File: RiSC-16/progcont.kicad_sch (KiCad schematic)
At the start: 9 parts, among them U6 74LS373, U7 74LS257, U8 74LS373, U9 74LS257

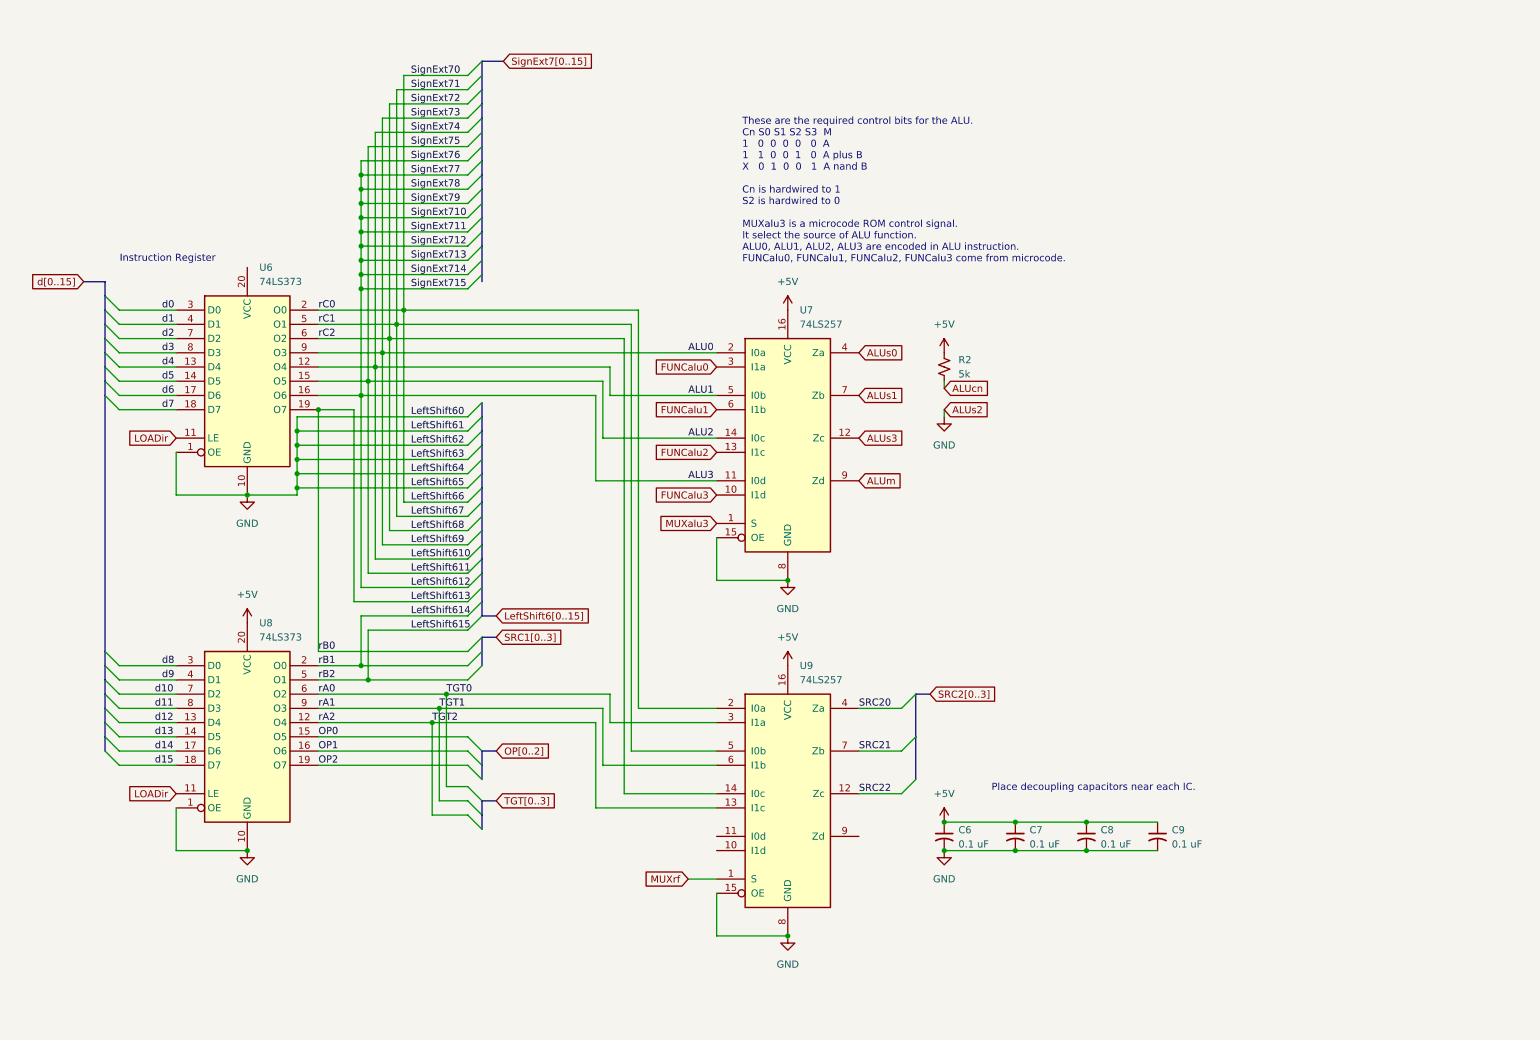
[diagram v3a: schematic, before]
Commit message: Refined instruction register.
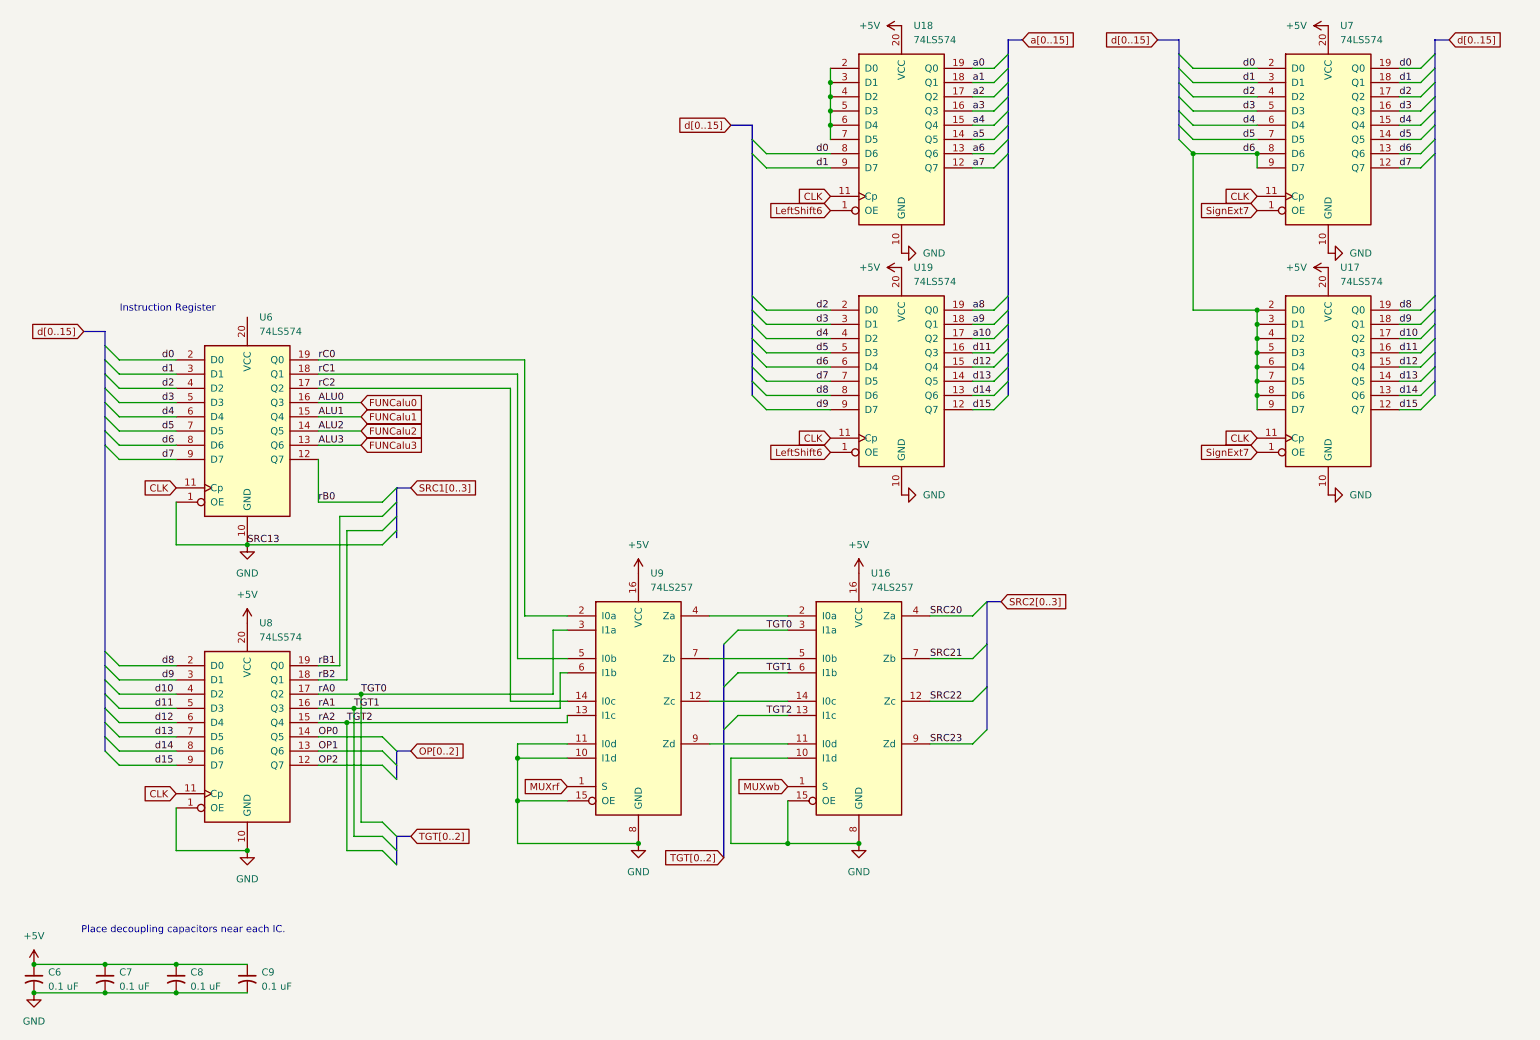
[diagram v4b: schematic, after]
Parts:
- removed R2: 5k, symbol Device:R_Small_US
- removed U6, U8: 74LS373, symbol 74xx:74LS373
- removed U7: 74LS257, symbol 74xx:74LS257
- added U16: 74LS257, symbol 74xx:74LS257
- added U17, U18, U19, U6, U7, U8: 74LS574, symbol 74xx:74LS574
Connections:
- net +5V: now also U16.16 (VCC), U17.20 (VCC), U18.20 (VCC), U19.20 (VCC), U7.20 (VCC), U8.20 (VCC)
- net FUNCalu0: now also U6.16 (Q3)
- net FUNCalu1: now also U6.15 (Q4)
- net FUNCalu2: now also U6.14 (Q5)
- net FUNCalu3: now also U6.13 (Q6)
- net GND: now also U9.10 (I1d), U9.11 (I0d), U16.10 (I1d), U16.15 (OE), U16.8 (GND), U17.10 (GND), U18.10 (GND), U19.10 (GND), U6.1 (OE), U6.10 (GND), U7.10 (GND), U8.1 (OE), U8.10 (GND)
- net OP0: now also U8.14 (Q5)
- net OP1: now also U8.13 (Q6)
- net OP2: now also U8.12 (Q7)
- net SRC20: now also U16.4 (Za); no longer U9.4 (Za)
- net SRC21: now also U16.7 (Zb); no longer U9.7 (Zb)
- net SRC22: now also U16.12 (Zc); no longer U9.12 (Zc)
- net TGT0: now also U16.3 (I1a), U8.17 (Q2)
- net TGT1: now also U16.6 (I1b), U8.16 (Q3)
- net TGT2: now also U16.13 (I1c), U8.15 (Q4)
- net d0: now also U18.8 (D6), U6.2 (D0), U7.19 (Q0), U7.2 (D0)
- net d1: now also U18.9 (D7), U6.3 (D1), U7.18 (Q1), U7.3 (D1)
- net d10: now also U17.17 (Q2), U8.4 (D2)
- net d11: now also U17.16 (Q3), U19.16 (Q3), U8.5 (D3)
- net d12: now also U17.15 (Q4), U19.15 (Q4), U8.6 (D4)
- net d13: now also U17.14 (Q5), U19.14 (Q5), U8.7 (D5)
- net d14: now also U17.13 (Q6), U19.13 (Q6), U8.8 (D6)
- net d15: now also U17.12 (Q7), U19.12 (Q7), U8.9 (D7)
- net d2: now also U19.2 (D0), U6.4 (D2), U7.17 (Q2), U7.4 (D2)
- net d3: now also U19.3 (D1), U6.5 (D3), U7.16 (Q3), U7.5 (D3)
- net d4: now also U19.4 (D2), U6.6 (D4), U7.15 (Q4), U7.6 (D4)
- net d5: now also U19.5 (D3), U6.7 (D5), U7.14 (Q5), U7.7 (D5)
- net d6: now also U17.2 (D0), U17.3 (D1), U17.4 (D2), U17.5 (D3), U17.6 (D4), U17.7 (D5), U17.8 (D6), U17.9 (D7), U19.6 (D4), U6.8 (D6), U7.13 (Q6), U7.8 (D6), U7.9 (D7)
- net d7: now also U19.7 (D5), U6.9 (D7), U7.12 (Q7)
- net d8: now also U17.19 (Q0), U19.8 (D6), U8.2 (D0)
- net d9: now also U17.18 (Q1), U19.9 (D7), U8.3 (D1)
- net at U9.9 (Zd): now also U16.11 (I0d)
- net LeftShift66 renamed rC0
- net rC0: now also U6.19 (Q0)
- net LeftShift67 renamed rC1
- net rC1: now also U6.18 (Q1)
- net LeftShift68 renamed rC2
- net rC2: now also U6.17 (Q2)
- new net: U18.2 (D0), U18.3 (D1), U18.4 (D2), U18.5 (D3), U18.6 (D4), U18.7 (D5)
- new net: U16.14 (I0c), U9.12 (Zc)
- new net: U16.2 (I0a), U9.4 (Za)
- new net: U16.5 (I0b), U9.7 (Zb)
- new net CLK: U17.11 (Cp), U18.11 (Cp), U19.11 (Cp), U6.11 (Cp), U7.11 (Cp), U8.11 (Cp)
- new net LeftShift6: U18.1 (OE), U19.1 (OE)
- new net MUXwb: U16.1 (S)
- new net SRC23: U16.9 (Zd)
- new net SignExt7: U17.1 (OE), U7.1 (OE)
- new net a0: U18.19 (Q0)
- new net a1: U18.18 (Q1)
- new net a10: U19.17 (Q2)
- new net a2: U18.17 (Q2)
- new net a3: U18.16 (Q3)
- new net a4: U18.15 (Q4)
- new net a5: U18.14 (Q5)
- new net a6: U18.13 (Q6)
- new net a7: U18.12 (Q7)
- new net a8: U19.19 (Q0)
- new net a9: U19.18 (Q1)
- new net rB0: U6.12 (Q7)
- new net rB1: U8.19 (Q0)
- new net rB2: U8.18 (Q1)
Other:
- note removed: "These are the required control bits for the ALU. Cn S0 S1 S2 S3 M 1 0 0 0 0 0 A 1 1 0 0 1 0 A plus B X 0 1 0 0 1 A nand B Cn is hardwired to 1 S2 is hardwired to 0 MUXalu3 is a microcode ROM control signal. It select the source of ALU function. ALU0, ALU1, ALU2, ALU3 are encoded in ALU instruction. FUNCalu0, FUNCalu1, FUNCalu2, FUNCalu3 come from microcode."
- moved on the sheet: C6, C7, C8, C9, U9

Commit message: Continued on the instruction register and decoding.
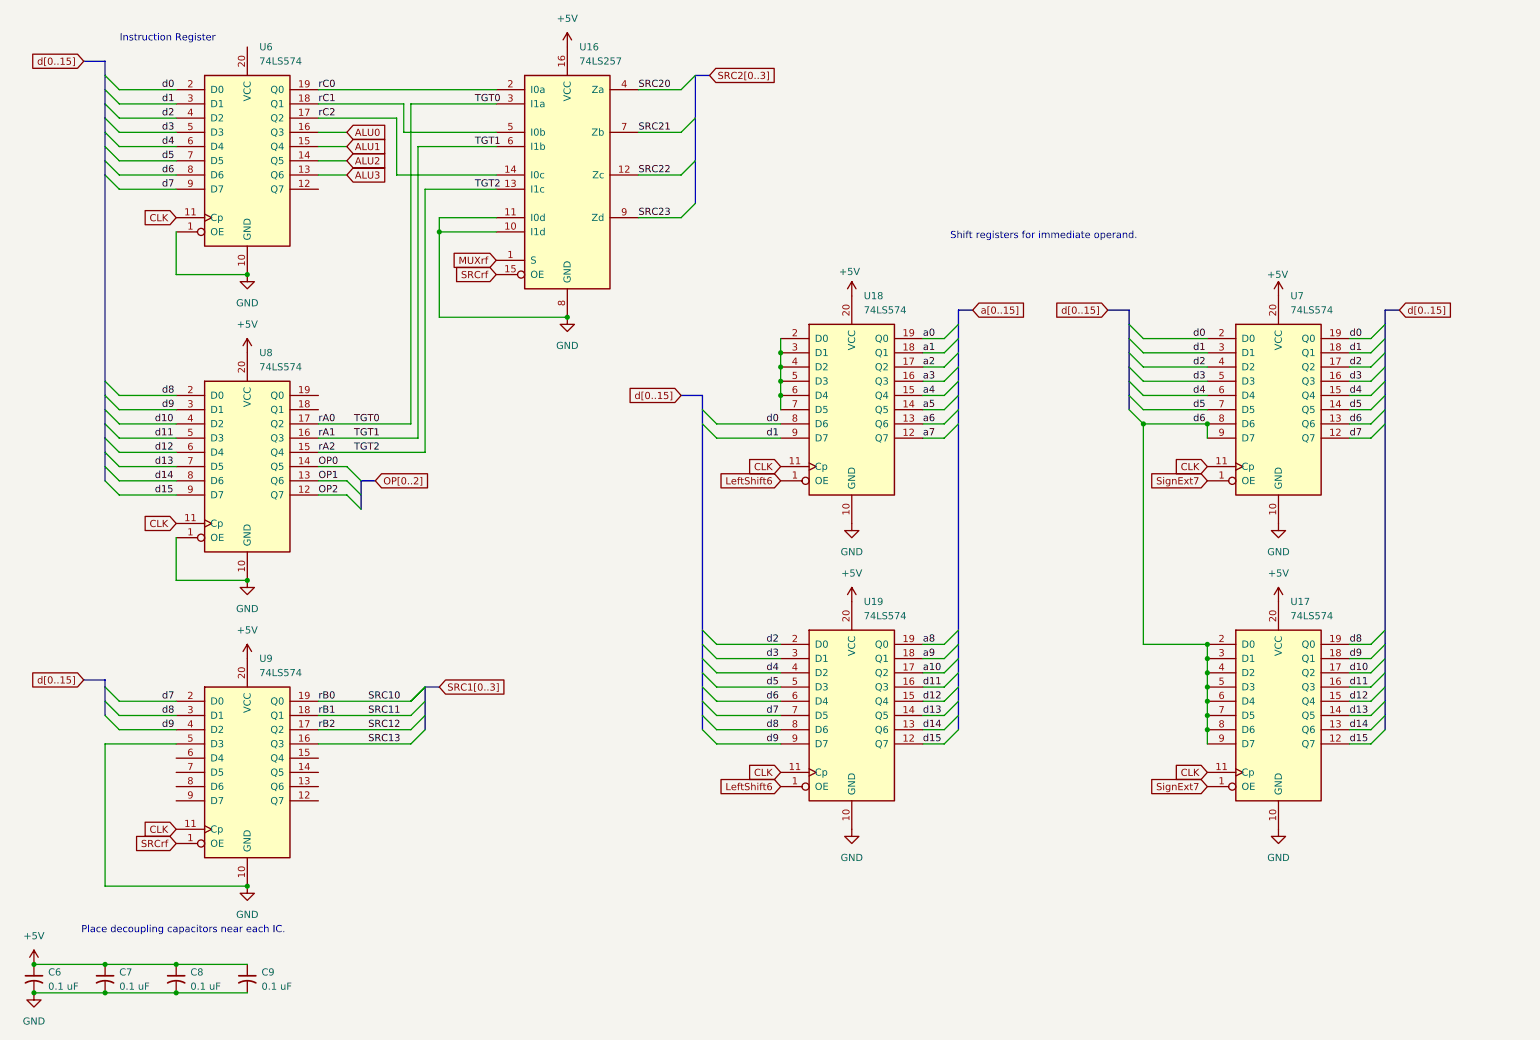
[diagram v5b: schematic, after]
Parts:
- removed U9: 74LS257, symbol 74xx:74LS257
- added U9: 74LS574, symbol 74xx:74LS574
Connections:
- net MUXwb is gone; now on net MUXrf: U16.1 (S)
- net +5V: now also U9.20 (VCC)
- net CLK: now also U9.11 (Cp)
- net GND: now also U16.11 (I0d), U9.10 (GND), U9.5 (D3); no longer U16.15 (OE)
- net d7: now also U9.2 (D0)
- net d8: now also U9.3 (D1)
- net d9: now also U9.4 (D2)
- net rC0: now also U16.2 (I0a)
- net rC1: now also U16.5 (I0b)
- net rC2: now also U16.14 (I0c)
- net FUNCalu0 renamed ALU0
- net FUNCalu1 renamed ALU1
- net FUNCalu2 renamed ALU2
- net FUNCalu3 renamed ALU3
- net rB0: no longer names the net of U6.12 (Q7)
- net rB1: no longer names the net of U8.19 (Q0)
- net rB2: no longer names the net of U8.18 (Q1)
- new net SRC10: U9.19 (Q0)
- new net SRC11: U9.18 (Q1)
- new net SRC12: U9.17 (Q2)
- new net SRC13: U9.16 (Q3)
- new net SRCrf: U16.15 (OE), U9.1 (OE)
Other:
- note added: "Shift registers for immediate operand."
- moved on the sheet: U16, U17, U18, U19, U6, U7, U8

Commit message: Annotated the schematic to align part numbers. EPROM and RAM board was added last revision. Reworked the src1 latching to assert 0xf to select the PC.
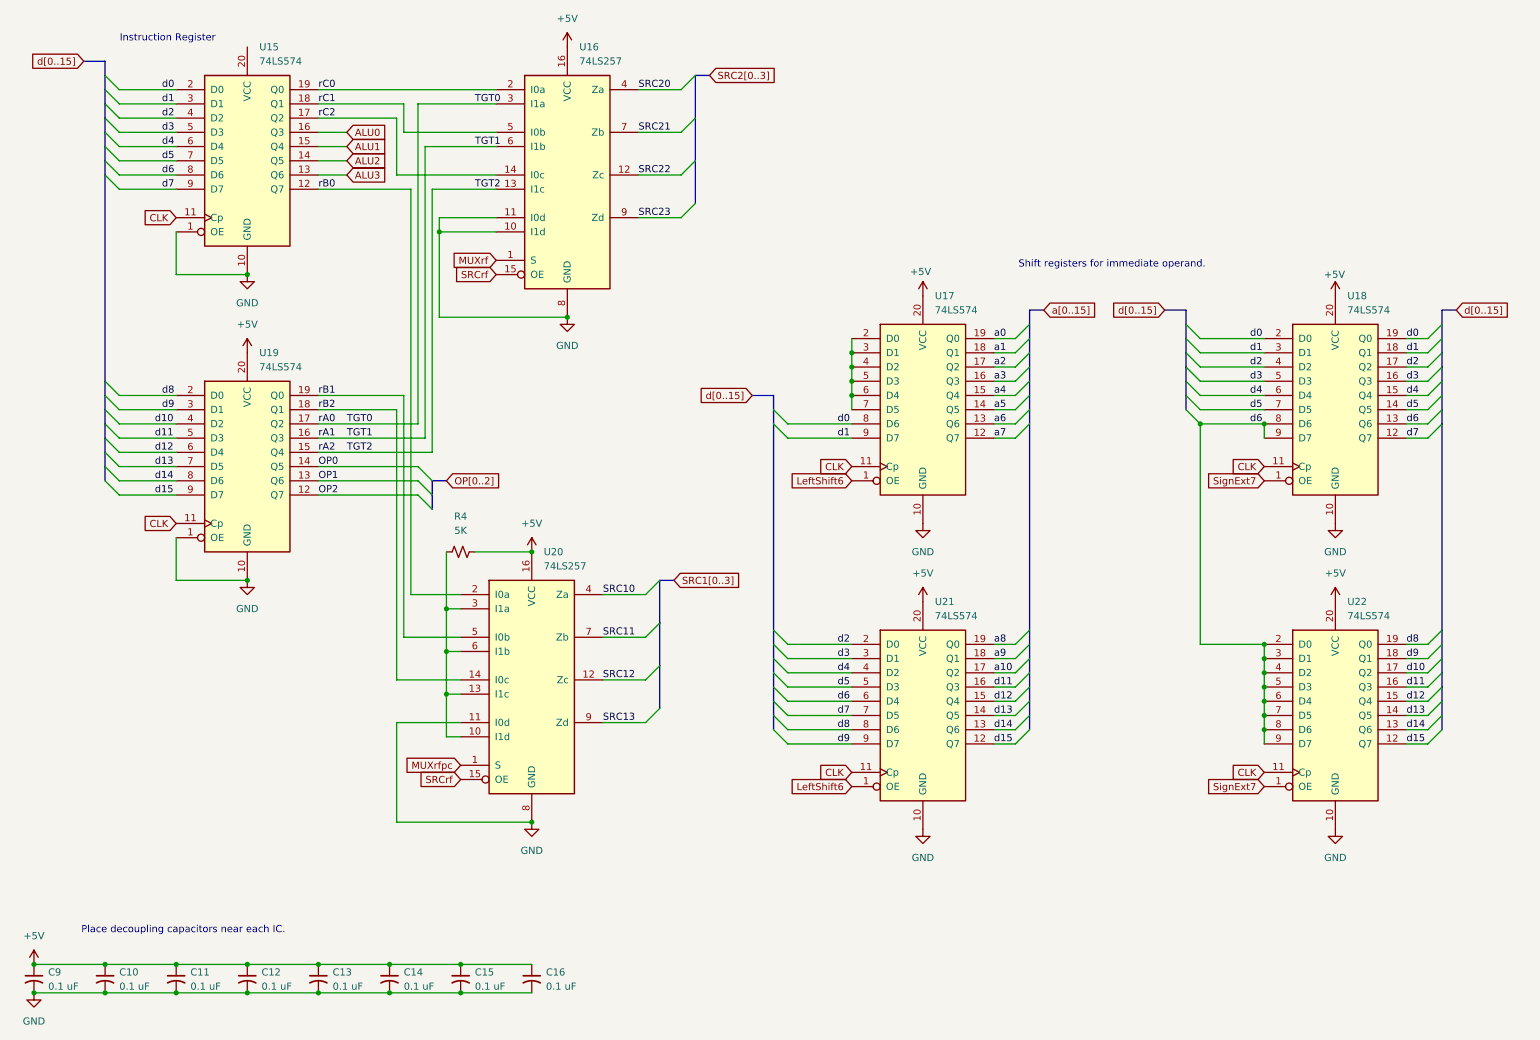
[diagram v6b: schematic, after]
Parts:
- removed U9: 74LS574, symbol 74xx:74LS574
- added C13, C14, C15, C16: 0.1 uF, symbol Device:C_Small_US
- added R4: 5K, symbol Device:R_Small_US
- added U20: 74LS257, symbol 74xx:74LS257
- renumbered C7 to C10, C8 to C11, C9 to C12, C6 to C9, U6 to U15, U18 to U17, U7 to U18, U8 to U19, U19 to U21, U17 to U22
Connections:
- net +5V: now also C13.1, C14.1, C15.1, C16.1, R4.1, U20.16 (VCC)
- net GND: now also C13.2, C14.2, C15.2, C16.2, U20.11 (I0d), U20.8 (GND)
- net SRC10: now also U20.4 (Za)
- net SRC11: now also U20.7 (Zb)
- net SRC12: now also U20.12 (Zc)
- net SRC13: now also U20.9 (Zd)
- net SRCrf: now also U20.15 (OE)
- net rB0: now reaches U15.12 (Q7)
- net rB0: now also U20.2 (I0a)
- net rB2: now reaches U19.18 (Q1)
- net rB2: now also U20.14 (I0c)
- net rB1: now reaches U19.19 (Q0)
- net rB1: now also U20.5 (I0b)
- new net: R4.2, U20.10 (I1d), U20.13 (I1c), U20.3 (I1a), U20.6 (I1b)
- new net MUXrfpc: U20.1 (S)
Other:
- moved on the sheet: U17, U18, U21, U22

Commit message: Minor edits
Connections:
- net at R4.2, U20.10 (I1d), U20.13 (I1c)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: no longer U20.3 (I1a)
- new net PCMAR: U20.3 (I1a)
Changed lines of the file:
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@@
 	)
 	(junction
-		(at 93.98 134.62)
-		(diameter 0)
-		(color 0 0 0 0)
-	)
-	(junction
 		(at 58.42 59.69)
 		(diameter 0)
@@
 	)
 	(junction
-		(at 93.98 127)
-		(diameter 0)
-		(color 0 0 0 0)
-	)
-	(junction
 		(at 71.12 182.88)
 		(diameter 0)
@@
 	)
 	(junction
-		(at 93.98 119.38)
-		(diameter 0)
-		(color 0 0 0 0)
-	)
-	(junction
 		(at 240.03 86.36)
 		(diameter 0)
@@
 	)
 	(junction
+		(at 82.55 134.62)
+		(diameter 0)
+		(color 0 0 0 0)
+	)
+	(junction
 		(at 166.37 78.74)
 		(diameter 0)
@@
 	)
 	(junction
+		(at 82.55 127)
+		(diameter 0)
+		(color 0 0 0 0)
+	)
+	(junction
 		(at 71.12 187.96)
 		(diameter 0)
@@
 	(wire
 		(pts
-			(xy 96.52 134.62) (xy 93.98 134.62)
-		)
-		(stroke
-			(width 0)
-			(type default)
-		)
-	)
-	(wire
-		(pts
 			(xy 228.6 83.82) (xy 240.03 83.82)
 		)
@@
 		)
 	)
+	(wire
+		(pts
+			(xy 82.55 109.22) (xy 93.98 109.22)
+		)
+		(stroke
+			(width 0)
+			(type default)
+		)
+	)
 	(bus
 		(pts
@@
 	(wire
 		(pts
-			(xy 93.98 119.38) (xy 93.98 127)
+			(xy 82.55 109.22) (xy 82.55 127)
 		)
 		(stroke
@@
 	(wire
 		(pts
-			(xy 71.12 83.82) (xy 85.09 83.82)
+			(xy 71.12 83.82) (xy 81.28 83.82)
 		)
 		(stroke
@@
 	(wire
 		(pts
-			(xy 93.98 134.62) (xy 93.98 142.24)
+			(xy 82.55 134.62) (xy 82.55 142.24)
 		)
 		(stroke
@@
 	(wire
 		(pts
-			(xy 93.98 142.24) (xy 96.52 142.24)
+			(xy 82.55 142.24) (xy 96.52 142.24)
 		)
 		(stroke
@@
 	(wire
 		(pts
-			(xy 71.12 44.45) (xy 87.63 44.45)
+			(xy 71.12 44.45) (xy 85.09 44.45)
 		)
 		(stroke
@@
 	(wire
 		(pts
-			(xy 86.36 124.46) (xy 96.52 124.46)
+			(xy 83.82 124.46) (xy 96.52 124.46)
 		)
 		(stroke
@@
 		)
 	)
+	(wire
+		(pts
+			(xy 82.55 134.62) (xy 96.52 134.62)
+		)
+		(stroke
+			(width 0)
+			(type default)
+		)
+	)
 	(bus
 		(pts
@@
 	(wire
 		(pts
-			(xy 87.63 116.84) (xy 96.52 116.84)
+			(xy 85.09 116.84) (xy 96.52 116.84)
 		)
 		(stroke
@@
 	(wire
 		(pts
-			(xy 87.63 44.45) (xy 87.63 116.84)
+			(xy 85.09 44.45) (xy 85.09 116.84)
 		)
 		(stroke
@@
 	(wire
 		(pts
-			(xy 71.12 187.96) (xy 83.82 187.96)
+			(xy 82.55 127) (xy 96.52 127)
 		)
 		(stroke
@@
 		)
 	)
-	(bus
+	(wire
 		(pts
-			(xy 33.02 34.29) (xy 33.02 36.83)
+			(xy 71.12 187.96) (xy 83.82 187.96)
 		)
 		(stroke
@@
 		)
 	)
-	(wire
+	(bus
 		(pts
-			(xy 96.52 119.38) (xy 93.98 119.38)
+			(xy 33.02 34.29) (xy 33.02 36.83)
 		)
 		(stroke
@@
 	(wire
 		(pts
-			(xy 71.12 81.28) (xy 86.36 81.28)
+			(xy 71.12 81.28) (xy 83.82 81.28)
 		)
 		(stroke
@@
 	(wire
 		(pts
-			(xy 85.09 83.82) (xy 85.09 132.08)
+			(xy 81.28 83.82) (xy 81.28 132.08)
 		)
 		(stroke
@@
 	(wire
 		(pts
-			(xy 93.98 127) (xy 93.98 134.62)
-		)
-		(stroke
-			(width 0)
-			(type default)
-		)
-	)
-	(wire
-		(pts
-			(xy 93.98 127) (xy 96.52 127)
+			(xy 82.55 127) (xy 82.55 134.62)
 		)
 		(stroke
@@
 	(wire
 		(pts
-			(xy 85.09 132.08) (xy 96.52 132.08)
+			(xy 81.28 132.08) (xy 96.52 132.08)
 		)
 		(stroke
@@
 	(wire
 		(pts
-			(xy 93.98 109.22) (xy 93.98 119.38)
-		)
-		(stroke
-			(width 0)
-			(type default)
-		)
-	)
-	(wire
-		(pts
 			(xy 91.44 91.44) (xy 91.44 44.45)
 		)
@@
 	(wire
 		(pts
-			(xy 86.36 81.28) (xy 86.36 124.46)
+			(xy 83.82 81.28) (xy 83.82 124.46)
 		)
 		(stroke
@@
 				(hide yes)
 			)
+		)
+	)
+	(global_label "PCMAR"
+		(shape input)
+		(at 96.52 119.38 180)
+		(fields_autoplaced yes)
+		(effects
+			(font
+				(size 1.27 1.27)
+			)
+			(justify right)
+		)
+		(property "Intersheetrefs" "${INTERSHEET_REFS}"
+			(at 87.1848 119.38 0)
+			(effects
+				(font
+					(size 1.27 1.27)
+				)
+				(justify right)
+				(hide yes)
+			)
